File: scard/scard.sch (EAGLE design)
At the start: 21 parts, among them IC1 LT3434, IC2 LT3434, Q1 IRFD9210, X1 COAX

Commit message: tentatively completed battery charging IC supporting circuitry
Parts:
- removed C3: 10uF, resistor:C-USC0805
- added C5: 10uF, resistor:C-USC0805
- added L2: 10uH, Seeed-Inductor:SMD-FERRITE-BEAD-470R-2A(0805)'0805'
- added U$5: B085BM30, calsat:B085BM30
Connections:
- new net N$5: CHRG_IC.BAT, L2.2, R5.2, R7.2
- net +12V: now also U$1.@1, U$1.@2; no longer U$1.ANODE@1, U$1.ANODE@2
- net GND: now also C5.2, U$5.@1, U$5.@2; no longer C3.2
- net N$2: now also L2.1; no longer R7.1
- net N$3: now also U$3.@3; no longer U$4.CATHODE
- net N$4: now also U$5.@3
- net SYS_UNREG: now also U$1.@3, U$4.@3; no longer U$1.CATHODE, U$3.CATHODE
- net VBATT: now also C5.1, R7.1, U$3.@1, U$3.@2, U$4.@1, U$4.@2; no longer C3.1, CHRG_IC.BAT, R5.2, R7.2, U$3.ANODE@1, U$3.ANODE@2, U$4.ANODE@1, U$4.ANODE@2
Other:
- moved on the sheet: R5, R6, R7

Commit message: fixed sense resistor placement for charger
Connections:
- removed net N$5: CHRG_IC.BAT, L2.2, R5.2, R7.2
- new net N$6: L2.2, R7.2
- net VBATT: now also CHRG_IC.BAT, R5.2
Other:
- note added: "battery conn goes here"
- note added: "solar cell conn here"
- moved on the sheet: IC1, IC2, R5, R6
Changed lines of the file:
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@@
 <sheet>
 <plain>
+<text x="-68.58" y="-66.04" size="1.778" layer="94">battery conn goes here</text>
+<text x="-154.94" y="-5.08" size="1.778" layer="94">solar cell conn here</text>
 </plain>
 <instances>
@@
 <instance part="GND8" gate="1" x="-71.12" y="-17.78" rot="R180"/>
 <instance part="GND9" gate="1" x="-88.9" y="-66.04"/>
-<instance part="R5" gate="G$1" x="-76.2" y="-53.34" rot="R90"/>
-<instance part="R6" gate="G$1" x="-81.28" y="-60.96" rot="R180"/>
+<instance part="R5" gate="G$1" x="-78.74" y="-53.34" rot="R90"/>
+<instance part="R6" gate="G$1" x="-83.82" y="-60.96" rot="R180"/>
 <instance part="C4" gate="G$1" x="-55.88" y="-27.94"/>
-<instance part="IC1" gate="G$1" x="27.94" y="-20.32"/>
-<instance part="IC2" gate="G$1" x="27.94" y="-66.04"/>
+<instance part="IC1" gate="G$1" x="45.72" y="-20.32"/>
+<instance part="IC2" gate="G$1" x="45.72" y="-91.44"/>
 <instance part="U$1" gate="G$1" x="-111.76" y="0"/>
 <instance part="U$3" gate="G$1" x="-43.18" y="-33.02" rot="R90"/>
@@
 <wire x1="-109.22" y1="-50.8" x2="-88.9" y2="-50.8" width="0.1524" layer="91"/>
 <pinref part="R6" gate="G$1" pin="2"/>
-<wire x1="-86.36" y1="-60.96" x2="-88.9" y2="-60.96" width="0.1524" layer="91"/>
 <junction x="-88.9" y="-60.96"/>
 </segment>
@@
 <wire x1="-27.94" y1="0" x2="-38.1" y2="0" width="0.1524" layer="91"/>
 <junction x="-27.94" y="0"/>
-<pinref part="IC1" gate="G$1" pin="VIN@1"/>
 <wire x1="-27.94" y1="0" x2="-15.24" y2="0" width="0.1524" layer="91"/>
 <wire x1="-15.24" y1="0" x2="12.7" y2="0" width="0.1524" layer="91"/>
-<wire x1="12.7" y1="0" x2="12.7" y2="-5.08" width="0.1524" layer="91"/>
-<pinref part="IC1" gate="G$1" pin="VIN@2"/>
-<wire x1="12.7" y1="-5.08" x2="12.7" y2="-7.62" width="0.1524" layer="91"/>
-<junction x="12.7" y="-5.08"/>
-<wire x1="-15.24" y1="0" x2="-15.24" y2="-50.8" width="0.1524" layer="91"/>
+<wire x1="-15.24" y1="0" x2="-15.24" y2="-76.2" width="0.1524" layer="91"/>
 <junction x="-15.24" y="0"/>
-<pinref part="IC2" gate="G$1" pin="VIN@1"/>
-<wire x1="-15.24" y1="-50.8" x2="12.7" y2="-50.8" width="0.1524" layer="91"/>
-<pinref part="IC2" gate="G$1" pin="VIN@2"/>
-<wire x1="12.7" y1="-50.8" x2="12.7" y2="-53.34" width="0.1524" layer="91"/>
-<junction x="12.7" y="-50.8"/>
 <pinref part="U$1" gate="G$1" pin="@3"/>
 <pinref part="U$4" gate="G$1" pin="@3"/>
 <wire x1="-27.94" y1="-27.94" x2="-27.94" y2="0" width="0.1524" layer="91"/>
+<pinref part="IC1" gate="G$1" pin="VIN@2"/>
+<pinref part="IC1" gate="G$1" pin="VIN@1"/>
+<wire x1="30.48" y1="-5.08" x2="30.48" y2="-7.62" width="0.1524" layer="91"/>
+<wire x1="12.7" y1="0" x2="12.7" y2="-5.08" width="0.1524" layer="91"/>
+<wire x1="12.7" y1="-5.08" x2="30.48" y2="-5.08" width="0.1524" layer="91"/>
+<junction x="30.48" y="-5.08"/>
+<pinref part="IC2" gate="G$1" pin="VIN@2"/>
+<pinref part="IC2" gate="G$1" pin="VIN@1"/>
+<wire x1="30.48" y1="-76.2" x2="30.48" y2="-78.74" width="0.1524" layer="91"/>
+<wire x1="-15.24" y1="-76.2" x2="30.48" y2="-76.2" width="0.1524" layer="91"/>
+<junction x="30.48" y="-76.2"/>
 </segment>
 </net>
@@
 <junction x="-68.58" y="-58.42"/>
 <wire x1="-43.18" y1="-58.42" x2="-68.58" y2="-58.42" width="0.1524" layer="91"/>
+<wire x1="-68.58" y1="-58.42" x2="-73.66" y2="-58.42" width="0.1524" layer="91"/>
+<pinref part="R5" gate="G$1" pin="2"/>
+<pinref part="CHRG_IC" gate="G$1" pin="BAT"/>
+<wire x1="-91.44" y1="-40.64" x2="-91.44" y2="-48.26" width="0.1524" layer="91"/>
+<wire x1="-91.44" y1="-48.26" x2="-78.74" y2="-48.26" width="0.1524" layer="91"/>
+<wire x1="-73.66" y1="-58.42" x2="-73.66" y2="-48.26" width="0.1524" layer="91"/>
+<wire x1="-73.66" y1="-48.26" x2="-78.74" y2="-48.26" width="0.1524" layer="91"/>
+<junction x="-78.74" y="-48.26"/>
 </segment>
 </net>
@@
 <pinref part="R5" gate="G$1" pin="1"/>
 <pinref part="R6" gate="G$1" pin="1"/>
-<wire x1="-76.2" y1="-58.42" x2="-76.2" y2="-60.96" width="0.1524" layer="91"/>
-<wire x1="-76.2" y1="-60.96" x2="-76.2" y2="-71.12" width="0.1524" layer="91"/>
-<junction x="-76.2" y="-60.96"/>
+<wire x1="-78.74" y1="-58.42" x2="-78.74" y2="-60.96" width="0.1524" layer="91"/>
+<wire x1="-78.74" y1="-60.96" x2="-78.74" y2="-71.12" width="0.1524" layer="91"/>
+<junction x="-78.74" y="-60.96"/>
 <pinref part="CHRG_IC" gate="G$1" pin="V_FB"/>
-<wire x1="-76.2" y1="-71.12" x2="-127" y2="-71.12" width="0.1524" layer="91"/>
+<wire x1="-78.74" y1="-71.12" x2="-127" y2="-71.12" width="0.1524" layer="91"/>
 <wire x1="-127" y1="-71.12" x2="-127" y2="-40.64" width="0.1524" layer="91"/>
 <label x="-127" y="-60.96" size="1.778" layer="95" rot="R90"/>
@@
 </segment>
 </net>
-<net name="N$5" class="0">
-<segment>
-<pinref part="R5" gate="G$1" pin="2"/>
-<pinref part="CHRG_IC" gate="G$1" pin="BAT"/>
-<wire x1="-91.44" y1="-40.64" x2="-91.44" y2="-48.26" width="0.1524" layer="91"/>
-<wire x1="-91.44" y1="-48.26" x2="-76.2" y2="-48.26" width="0.1524" layer="91"/>
-<junction x="-76.2" y="-48.26"/>
-<wire x1="-76.2" y1="-48.26" x2="-68.58" y2="-48.26" width="0.1524" layer="91"/>
-<pinref part="R7" gate="G$1" pin="2"/>
-<pinref part="L2" gate="L" pin="2"/>
-<wire x1="-68.58" y1="-48.26" x2="-68.58" y2="-45.72" width="0.1524" layer="91"/>
-<junction x="-68.58" y="-48.26"/>
-</segment>
-</net>
 <net name="N$2" class="0">
 <segment>
@@
 </segment>
 </net>
+<net name="N$6" class="0">
+<segment>
+<pinref part="L2" gate="L" pin="2"/>
+<pinref part="R7" gate="G$1" pin="2"/>
+<wire x1="-68.58" y1="-48.26" x2="-68.58" y2="-45.72" width="0.1524" layer="91"/>
+</segment>
+</net>

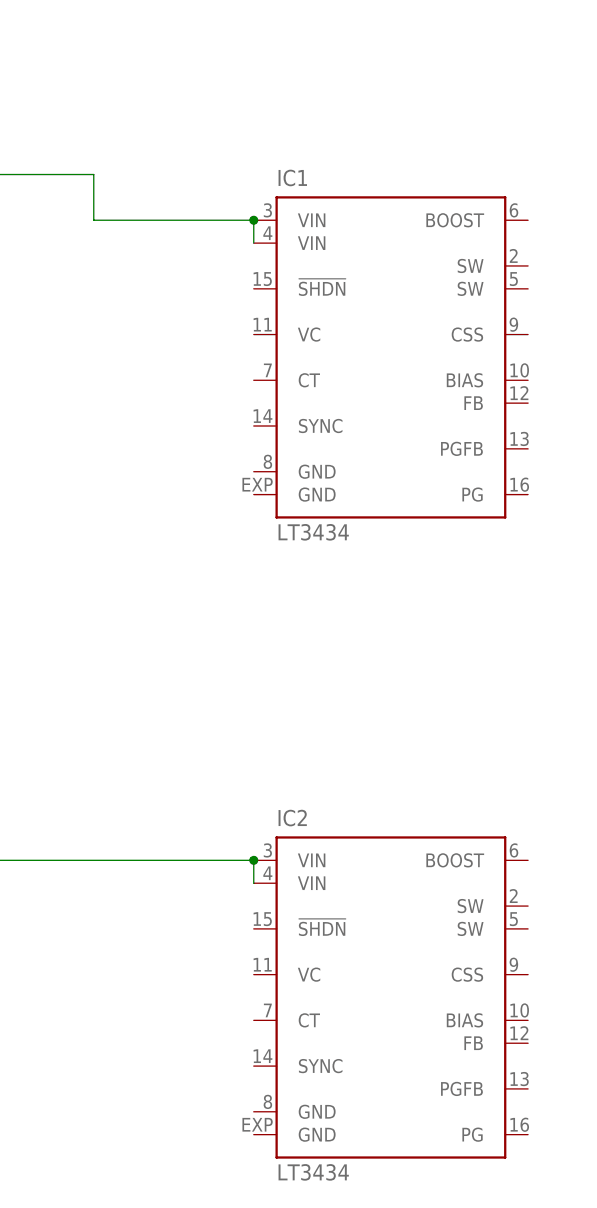
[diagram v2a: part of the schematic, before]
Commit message: finished adding tps63070 switching regulator
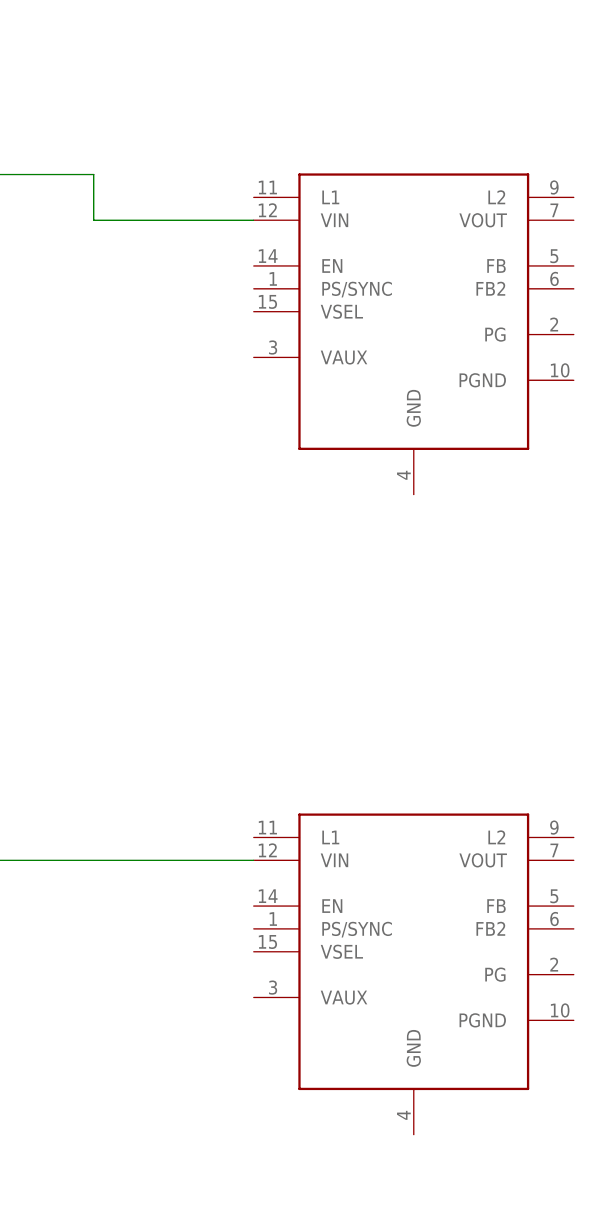
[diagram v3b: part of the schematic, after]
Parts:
- removed IC1, IC2: LT3434, linear-technology:LT3434
- added U$6, U$7: TPS63070, calsat:TPS63070
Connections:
- net SYS_UNREG: now also U$6.VIN, U$7.VIN; no longer IC1.VIN@1, IC1.VIN@2, IC2.VIN@1, IC2.VIN@2
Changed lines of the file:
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@@
 <part name="R6" library="resistor" library_urn="urn:adsk.eagle:library:348" deviceset="R-US_" device="R0402" value="~410k"/>
 <part name="C4" library="resistor" library_urn="urn:adsk.eagle:library:348" deviceset="C-US" device="C0805" value="1uF"/>
-<part name="IC1" library="linear-technology" library_urn="urn:adsk.eagle:library:261" deviceset="LT3434" device=""/>
-<part name="IC2" library="linear-technology" library_urn="urn:adsk.eagle:library:261" deviceset="LT3434" device=""/>
 <part name="U$1" library="calsat" deviceset="B085BM30" device=""/>
 <part name="U$3" library="calsat" deviceset="B085BM30" device=""/>
@@
 <part name="GND11" library="supply1" library_urn="urn:adsk.eagle:library:371" deviceset="GND" device=""/>
 <part name="L2" library="Seeed-Inductor" library_urn="urn:adsk.eagle:library:471" deviceset="SMD-FERRITE-BEAD-470R-2A(0805)" device="'0805'" value="10uH"/>
+<part name="U$6" library="calsat" deviceset="TPS63070" device=""/>
+<part name="U$7" library="calsat" deviceset="TPS63070" device=""/>
 </parts>
 <sheets>
@@
 <instance part="R6" gate="G$1" x="-83.82" y="-60.96" rot="R180"/>
 <instance part="C4" gate="G$1" x="-55.88" y="-27.94"/>
-<instance part="IC1" gate="G$1" x="45.72" y="-20.32"/>
-<instance part="IC2" gate="G$1" x="45.72" y="-91.44"/>
 <instance part="U$1" gate="G$1" x="-111.76" y="0"/>
 <instance part="U$3" gate="G$1" x="-43.18" y="-33.02" rot="R90"/>
@@
 <instance part="GND11" gate="1" x="-55.88" y="-50.8"/>
 <instance part="L2" gate="L" x="-68.58" y="-40.64" rot="R270"/>
+<instance part="U$6" gate="G$1" x="48.26" y="-15.24"/>
+<instance part="U$7" gate="G$1" x="48.26" y="-86.36"/>
 </instances>
 <busses>
@@
 <pinref part="U$4" gate="G$1" pin="@3"/>
 <wire x1="-27.94" y1="-27.94" x2="-27.94" y2="0" width="0.1524" layer="91"/>
-<pinref part="IC1" gate="G$1" pin="VIN@2"/>
-<pinref part="IC1" gate="G$1" pin="VIN@1"/>
-<wire x1="30.48" y1="-5.08" x2="30.48" y2="-7.62" width="0.1524" layer="91"/>
 <wire x1="12.7" y1="0" x2="12.7" y2="-5.08" width="0.1524" layer="91"/>
 <wire x1="12.7" y1="-5.08" x2="30.48" y2="-5.08" width="0.1524" layer="91"/>
-<junction x="30.48" y="-5.08"/>
-<pinref part="IC2" gate="G$1" pin="VIN@2"/>
-<pinref part="IC2" gate="G$1" pin="VIN@1"/>
-<wire x1="30.48" y1="-76.2" x2="30.48" y2="-78.74" width="0.1524" layer="91"/>
 <wire x1="-15.24" y1="-76.2" x2="30.48" y2="-76.2" width="0.1524" layer="91"/>
-<junction x="30.48" y="-76.2"/>
-</segment>
-</net>
+<pinref part="U$6" gate="G$1" pin="VIN"/>
+<pinref part="U$7" gate="G$1" pin="VIN"/>
+</segment>
+</net>

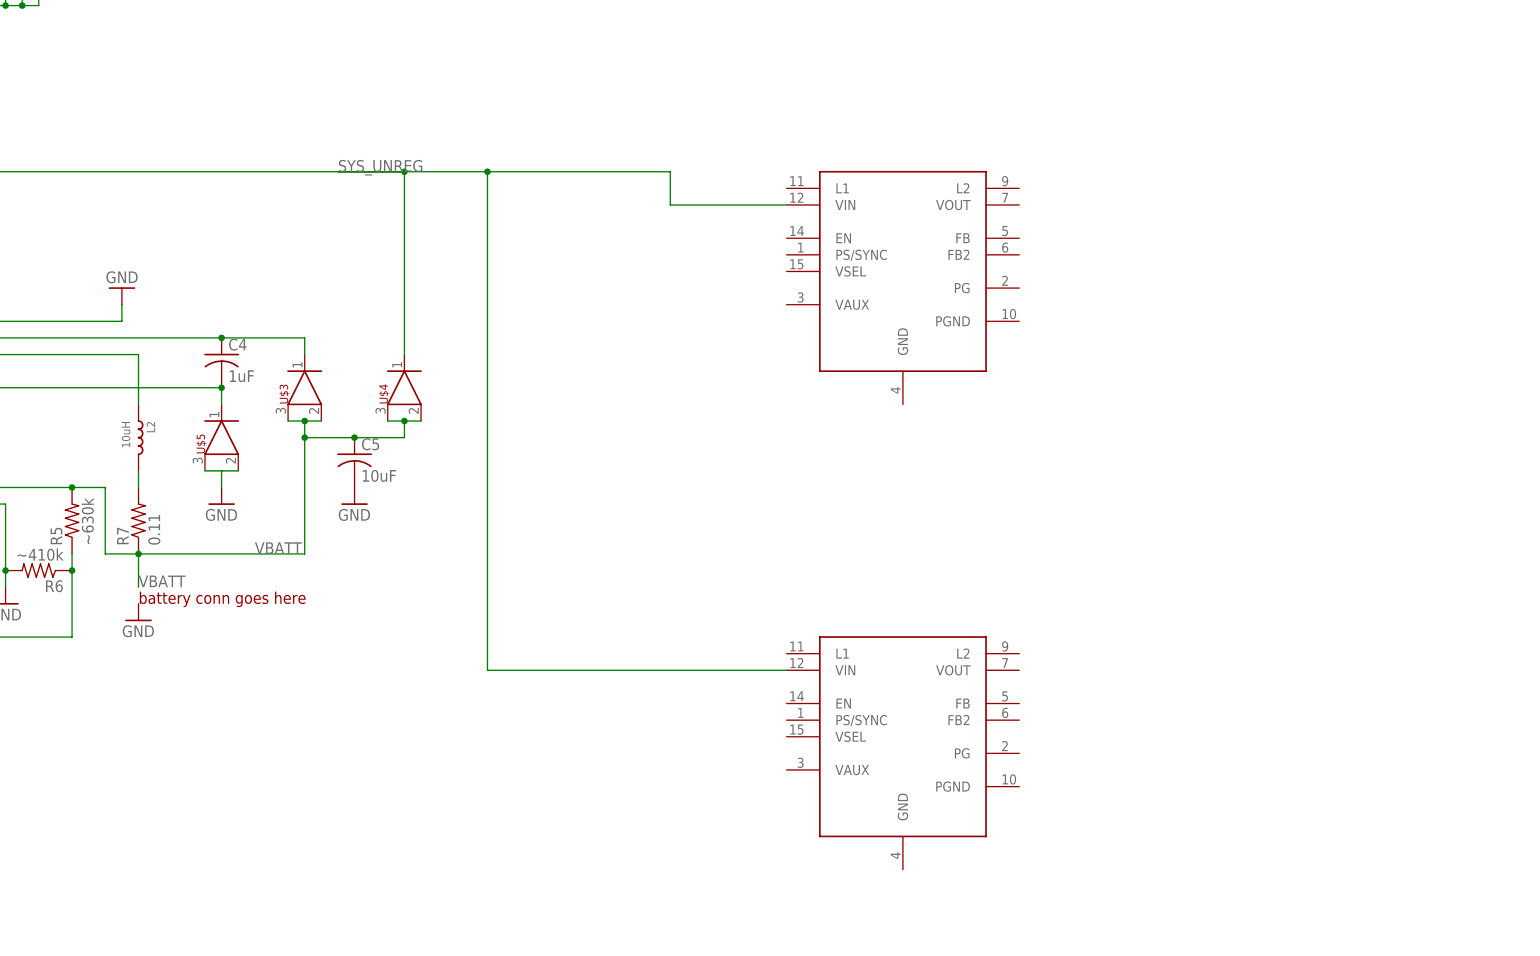
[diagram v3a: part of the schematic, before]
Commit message: added inductor part and completed schematic for 3v3 voltage regulators
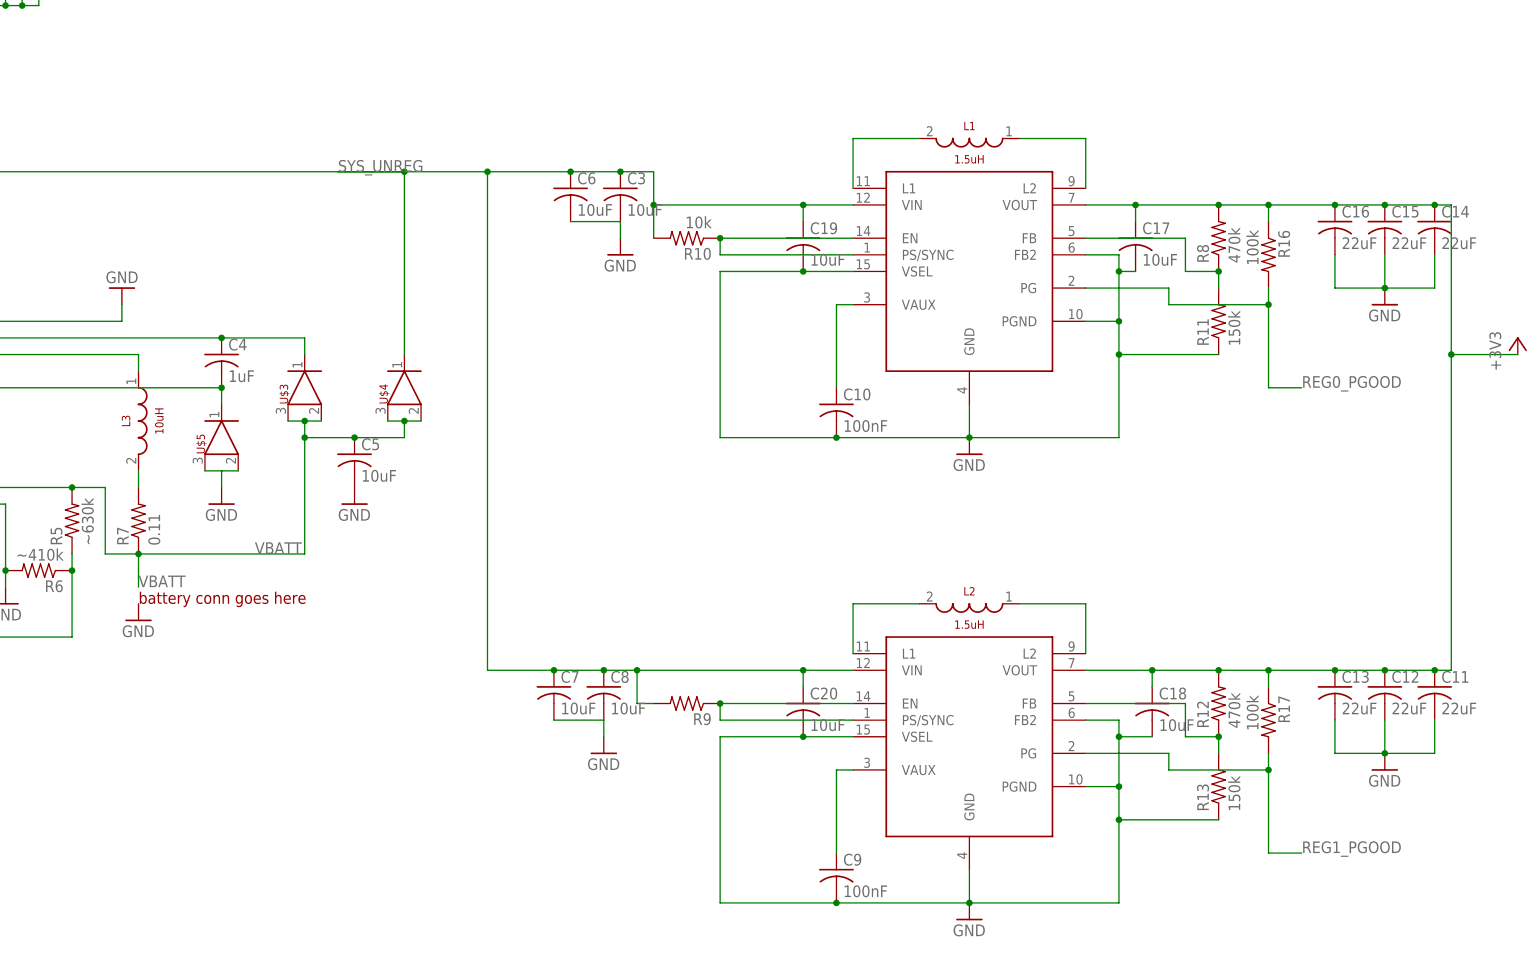
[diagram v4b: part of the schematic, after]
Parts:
- added C10, C9: 100nF, rcl:C-USC0603
- added C11, C12, C13, C14, C15, C16: 22uF, rcl:C-USC0805
- added C17, C18, C19, C20: 10uF, rcl:C-USC0603
- added C3, C6, C7, C8: 10uF, rcl:C-USC0805
- added L1: 1.5uH, calsat:XFL4020
- added L3: 10uH, calsat:XFL4020
- added R10: 10k, resistor:R-US_R0603
- added R11, R13: 150k, resistor:R-US_R0603
- added R12, R8: 470k, resistor:R-US_R0603
- added R16, R17: 100k, resistor:R-US_R0603
- added R9: (no value), resistor:R-US_R0603
- L2: value 10uH -> 1.5uH; device Seeed-Inductor:SMD-FERRITE-BEAD-470R-2A(0805)'0805' -> calsat:XFL4020
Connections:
- new net N$10: R12.1, R13.2, U$7.FB
- new net N$11: L2.@2, U$7.L1
- new net N$12: L2.@1, U$7.L2
- new net N$13: L1.@1, U$6.L2
- new net N$14: R11.2, R8.1, U$6.FB
- new net N$15: L1.@2, U$6.L1
- new net N$5: C9.1, U$7.VAUX
- new net N$9: C10.1, U$6.VAUX
- new net REG0_EN: R10.1, U$6.EN, U$6.PS/SYNC
- new net REG0_PGOOD: R16.2, U$6.PG
- new net REG1_EN: R9.1, U$7.EN, U$7.PS/SYNC
- new net REG1_PGOOD: R17.2, U$7.PG
- net +3V3: now also C11.1, C12.1, C13.1, C14.1, C15.1, C16.1, C17.1, C18.1, R12.2, R16.1, R17.1, R8.2, U$6.VOUT, U$7.VOUT
- net GND: now also C10.2, C11.2, C12.2, C13.2, C14.2, C15.2, C16.2, C17.2, C18.2, C19.2, C20.2, C6.2, C7.2, C8.2, C9.2, R11.1, R13.1, U$6.FB2, U$6.GND, U$6.PGND, U$6.VSEL, U$7.FB2, U$7.GND, U$7.PGND, U$7.VSEL
- net N$2: now also L3.@1; no longer L2.1
- net N$6: now also L3.@2; no longer L2.2
- net SYS_UNREG: now also C19.1, C20.1, C3.1, C6.1, C7.1, C8.1, R10.2, R9.2
